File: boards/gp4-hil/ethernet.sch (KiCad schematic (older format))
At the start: 63 parts, among them J1 BEL_FUSE_0826-1G1T-23-F, J3 XILINX_JTAG_ICESIDE, J4 XILINX_JTAG_ICESIDE, U2 XC7A100T-1FTG256C, U29 TXB0104RUT, U30 TXB0104RUT, U33 125 MHz, U5 KSZ9031RN, U7 25 MHz

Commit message: Added pulldown on ETH_RESET_N to ensure PHY stays in reset until FPGA initializes
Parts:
- added R187: 10K, symbol R
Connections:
- net ETH_RESET_N: now also R187.2
- net GND: now also R187.1
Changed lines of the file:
@@
 	11700 8500 11900 8500
 Wire Wire Line
-	12100 8600 11200 8600
+	11200 8600 12800 8600
 Wire Wire Line
 	11200 8500 11400 8500
@@
 Connection ~ 6850 6150
 Connection ~ 7750 6150
+$Comp
+L R R187
+U 1 1 57747EB0
+P 12800 8750
+F 0 "R187" H 12650 8750 50  0000 C CNN
+F 1 "10K" V 12800 8750 50  0000 C CNN
+F 2 "" V 12730 8750 30  0000 C CNN
+F 3 "" H 12800 8750 30  0000 C CNN
+	1    12800 8750
+	-1   0    0    1
+$EndComp
+Text Label 12650 8900 2    60   ~ 0
+GND
+Wire Wire Line
+	12650 8900 12800 8900
 $EndSCHEMATC

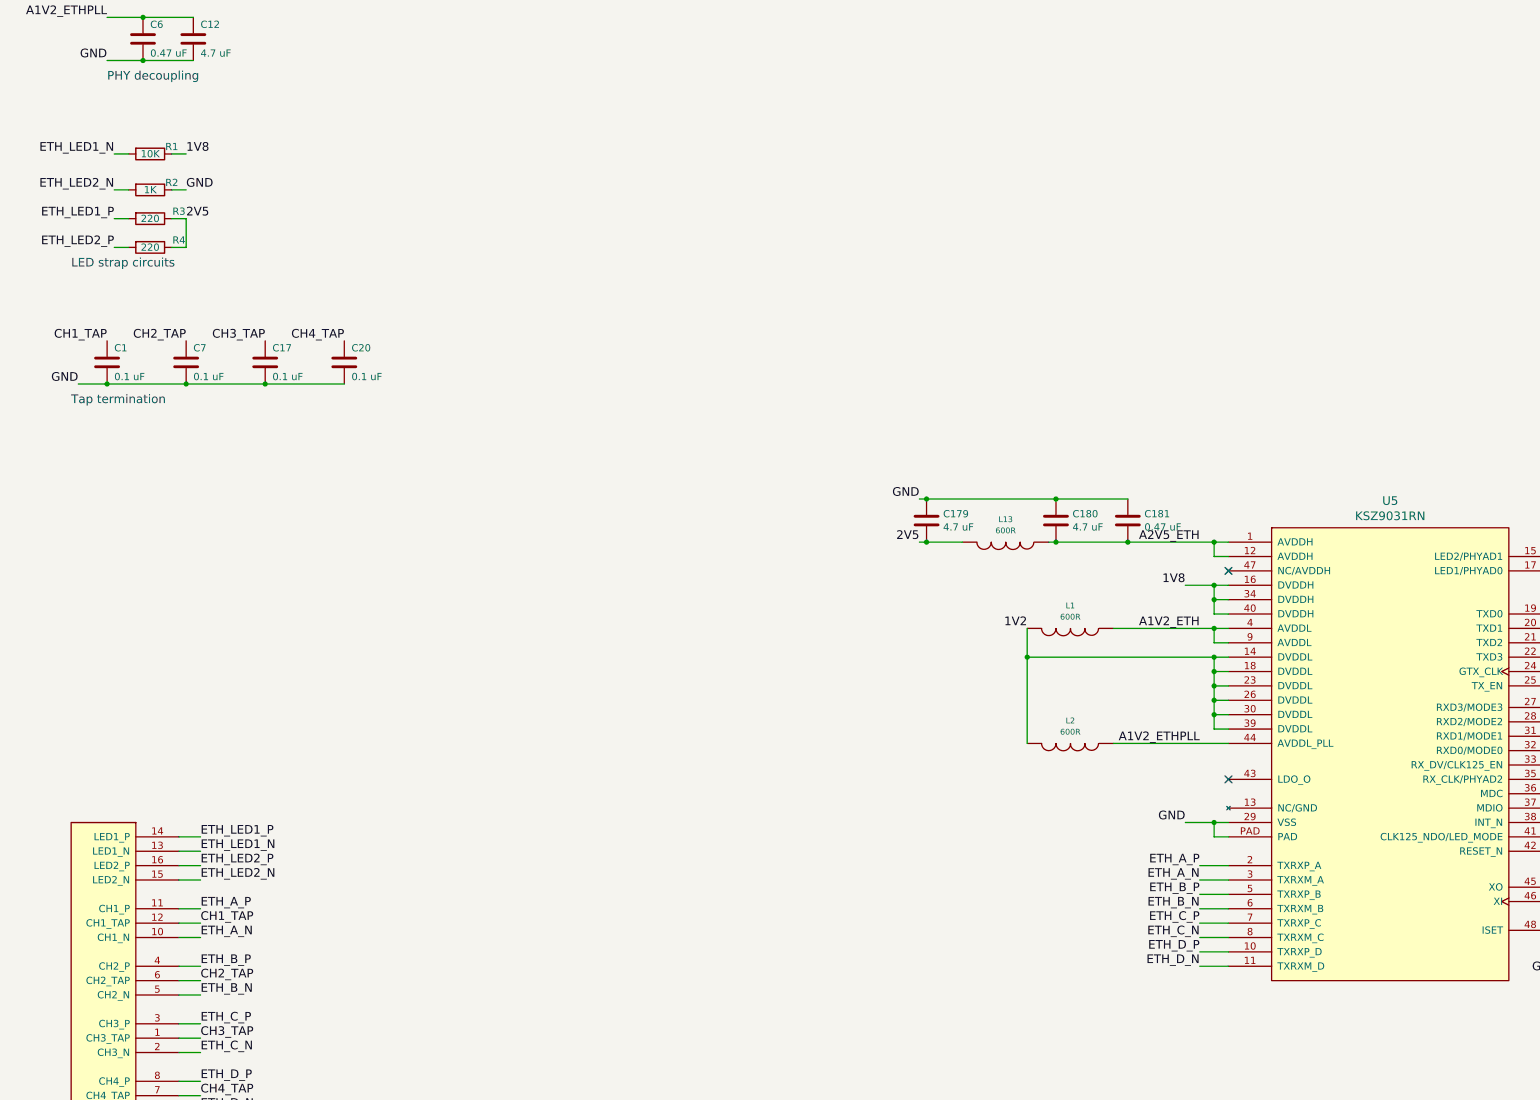
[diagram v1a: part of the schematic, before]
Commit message: Added PHY_MDC strap for PHY address configuration
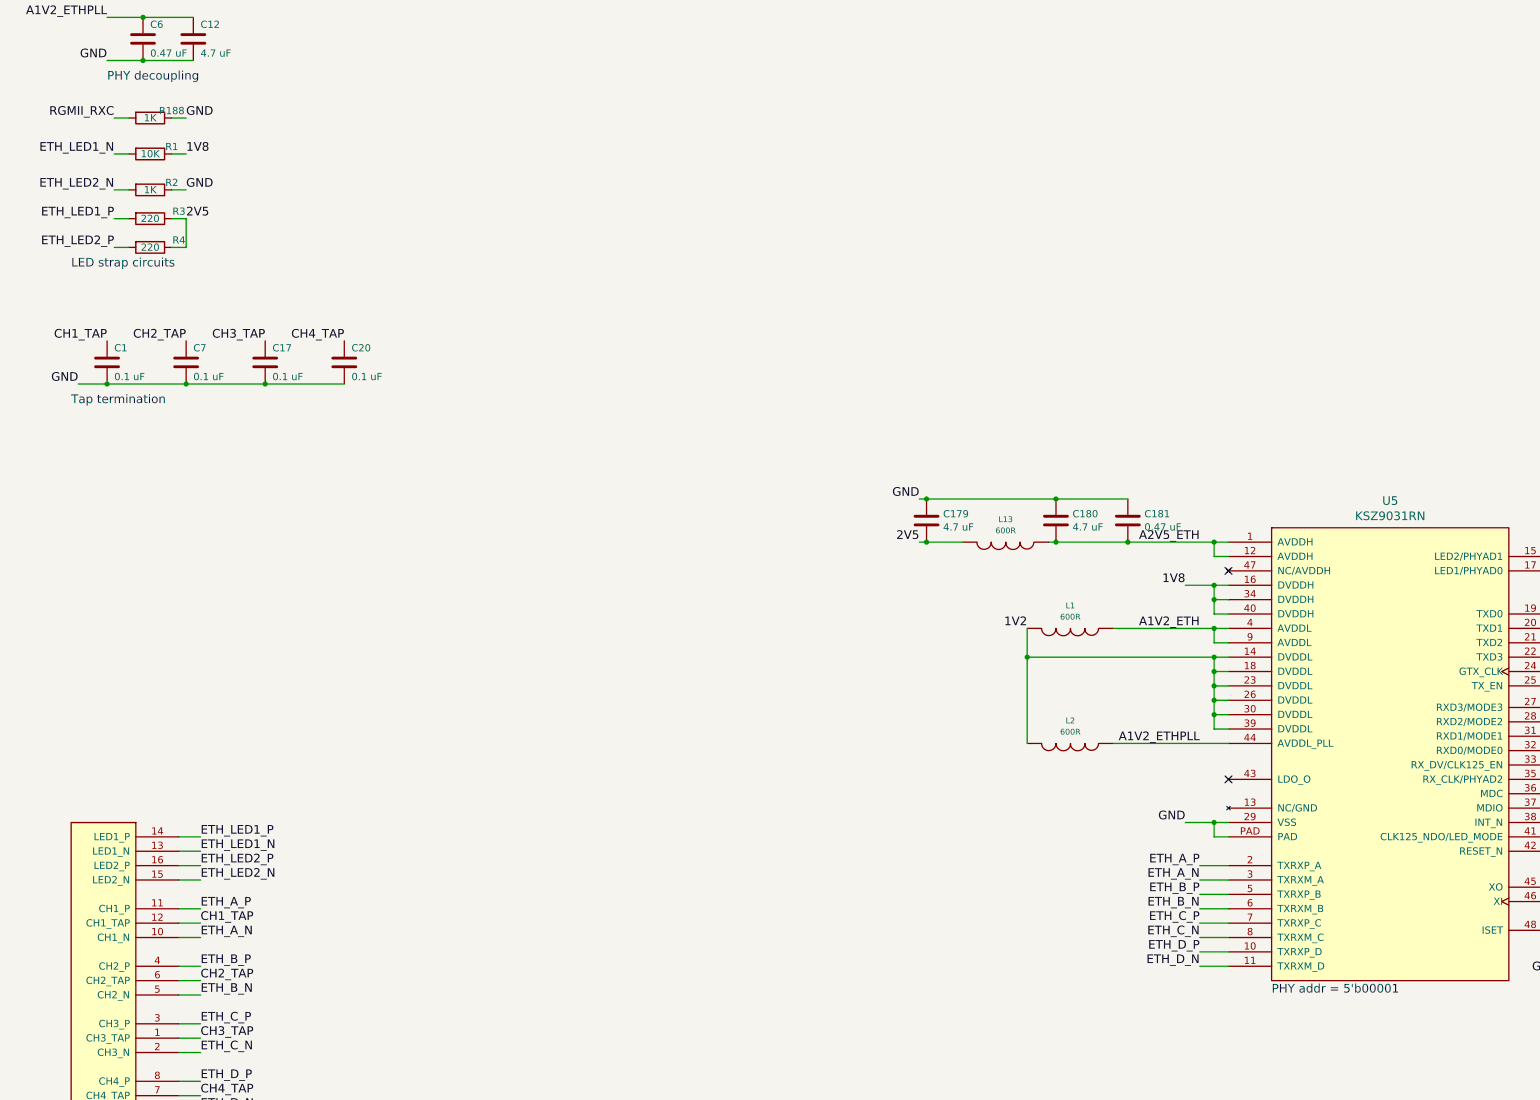
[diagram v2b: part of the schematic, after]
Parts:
- added R188: 1K, symbol R
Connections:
- net GND: now also R188.1
- net RGMII_RXC: now also R188.2
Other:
- note added: "PHY addr = 5'b00001"
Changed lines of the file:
@@
 Wire Wire Line
 	12650 8900 12800 8900
+Text Label 1200 3500 2    60   ~ 0
+RGMII_RXC
+$Comp
+L R R188
+U 1 1 57758CA7
+P 1450 3500
+F 0 "R188" V 1400 3650 50  0000 C CNN
+F 1 "1K" V 1450 3500 50  0000 C CNN
+F 2 "" V 1380 3500 30  0000 C CNN
+F 3 "" H 1450 3500 30  0000 C CNN
+	1    1450 3500
+	0    1    1    0
+$EndComp
+Wire Wire Line
+	1200 3500 1300 3500
+Text Label 1700 3500 0    60   ~ 0
+GND
+Wire Wire Line
+	1700 3500 1600 3500
+Text Notes 9250 9600 0    60   ~ 0
+PHY addr = 5'b00001
 $EndSCHEMATC

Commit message: Began work on footprint creation for layout.
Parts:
- C1, C10, C11, C14, C16, C163, C164, C165, C166, C17, C175, C181, C19, C2, C20, C21, C22, C24, C3, C4, C5, C6, C7, C8, C9: footprint (none) -> azonenberg_pcb:EIA_0402_CAP_NOSILK
- C12, C13, C15, C179, C18, C180, C23: footprint (none) -> azonenberg_pcb:EIA_0603_CAP_NOSILK
- J1: footprint (none) -> azonenberg_pcb:CONN_BELFUSE_0826_1G1T_23_F
- J3, J4: footprint (none) -> azonenberg_pcb:XILINX_JTAG_PTH_MOLEX_0878311420
- L1, L13, L2: footprint (none) -> azonenberg_pcb:EIA_0805_INDUCTOR_NOSILK
- TP22, TP23: footprint (none) -> azonenberg_pcb:TESTPOINT_SMT_KEYSTONE_5016
- U5: footprint (none) -> azonenberg_pcb:QFN_48_0.5MM_7x7MM

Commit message: Updated PCB with a lot more component footprints
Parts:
- L1, L13, L2: footprint azonenberg_pcb:EIA_0805_INDUCTOR_NOSILK -> azonenberg_pcb:EIA_0603_INDUCTOR_NOSILK
- R1, R10, R11, R12, R13, R14, R15, R150, R16, R187, R188, R2, R3, R4, R5, R6, R7, R8, R9: footprint (none) -> azonenberg_pcb:EIA_0402_RES_NOSILK
- U2: footprint (none) -> azonenberg_pcb:BGA_256_17x17_FULLARRAY_1MM
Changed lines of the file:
@@
 Sheet 3 7
 Title "GreenPak Hardware-In-Loop Test Platform"
-Date "2016-05-19"
+Date "2016-05-20"
 Rev "0.1"
 Comp "Andrew Zonenberg"
@@
 F 0 "R1" V 1400 3900 50  0000 C CNN
 F 1 "10K" V 1450 3750 50  0000 C CNN
-F 2 "" V 1380 3750 30  0001 C CNN
+F 2 "azonenberg_pcb:EIA_0402_RES_NOSILK" V 1380 3750 30  0001 C CNN
 F 3 "" H 1450 3750 30  0000 C CNN
 	1    1450 3750
@@
 F 0 "R2" V 1400 4150 50  0000 C CNN
 F 1 "1K" V 1450 4000 50  0000 C CNN
-F 2 "" V 1380 4000 30  0001 C CNN
+F 2 "azonenberg_pcb:EIA_0402_RES_NOSILK" V 1380 4000 30  0001 C CNN
 F 3 "" H 1450 4000 30  0000 C CNN
 	1    1450 4000
@@
 F 0 "R3" V 1400 4400 50  0000 C CNN
 F 1 "220" V 1450 4200 50  0000 C CNN
-F 2 "" V 1380 4200 30  0001 C CNN
+F 2 "azonenberg_pcb:EIA_0402_RES_NOSILK" V 1380 4200 30  0001 C CNN
 F 3 "" H 1450 4200 30  0000 C CNN
 	1    1450 4200
@@
 F 0 "R4" V 1400 4600 50  0000 C CNN
 F 1 "220" V 1450 4400 50  0000 C CNN
-F 2 "" V 1380 4400 30  0001 C CNN
+F 2 "azonenberg_pcb:EIA_0402_RES_NOSILK" V 1380 4400 30  0001 C CNN
 F 3 "" H 1450 4400 30  0000 C CNN
 	1    1450 4400
@@
 F 0 "L2" V 7692 7850 40  0000 C CNN
 F 1 "600R" V 7770 7850 40  0000 C CNN
-F 2 "azonenberg_pcb:EIA_0805_INDUCTOR_NOSILK" H 7850 7850 60  0001 C CNN
+F 2 "azonenberg_pcb:EIA_0603_INDUCTOR_NOSILK" H 7850 7850 60  0001 C CNN
 F 3 "" H 7850 7850 60  0000 C CNN
 	1    7850 7850
@@
 F 0 "L1" V 7692 7050 40  0000 C CNN
 F 1 "600R" V 7770 7050 40  0000 C CNN
-F 2 "azonenberg_pcb:EIA_0805_INDUCTOR_NOSILK" H 7850 7050 60  0001 C CNN
+F 2 "azonenberg_pcb:EIA_0603_INDUCTOR_NOSILK" H 7850 7050 60  0001 C CNN
 F 3 "" H 7850 7050 60  0000 C CNN
 	1    7850 7050
@@
 F 0 "R6" H 11470 9346 50  0000 L CNN
 F 1 "12.1k 1%" H 11470 9254 50  0000 L CNN
-F 2 "" V 11330 9300 30  0001 C CNN
+F 2 "azonenberg_pcb:EIA_0402_RES_NOSILK" V 11330 9300 30  0001 C CNN
 F 3 "" H 11400 9300 30  0000 C CNN
 	1    11400 9300
@@
 F 0 "R7" V 11500 7800 50  0000 C CNN
 F 1 "33" V 11550 7600 50  0000 C CNN
-F 2 "" V 11480 7600 30  0001 C CNN
+F 2 "azonenberg_pcb:EIA_0402_RES_NOSILK" V 11480 7600 30  0001 C CNN
 F 3 "" H 11550 7600 30  0000 C CNN
 	1    11550 7600
@@
 F 0 "R8" V 11500 7900 50  0000 C CNN
 F 1 "33" V 11550 7700 50  0000 C CNN
-F 2 "" V 11480 7700 30  0001 C CNN
+F 2 "azonenberg_pcb:EIA_0402_RES_NOSILK" V 11480 7700 30  0001 C CNN
 F 3 "" H 11550 7700 30  0000 C CNN
 	1    11550 7700
@@
 F 0 "R9" V 11500 8000 50  0000 C CNN
 F 1 "33" V 11550 7800 50  0000 C CNN
-F 2 "" V 11480 7800 30  0001 C CNN
+F 2 "azonenberg_pcb:EIA_0402_RES_NOSILK" V 11480 7800 30  0001 C CNN
 F 3 "" H 11550 7800 30  0000 C CNN
 	1    11550 7800
@@
 F 0 "R10" V 11500 8100 50  0000 C CNN
 F 1 "33" V 11550 7900 50  0000 C CNN
-F 2 "" V 11480 7900 30  0001 C CNN
+F 2 "azonenberg_pcb:EIA_0402_RES_NOSILK" V 11480 7900 30  0001 C CNN
 F 3 "" H 11550 7900 30  0000 C CNN
 	1    11550 7900
@@
 F 0 "R11" V 11500 8200 50  0000 C CNN
 F 1 "33" V 11550 8000 50  0000 C CNN
-F 2 "" V 11480 8000 30  0001 C CNN
+F 2 "azonenberg_pcb:EIA_0402_RES_NOSILK" V 11480 8000 30  0001 C CNN
 F 3 "" H 11550 8000 30  0000 C CNN
 	1    11550 8000
@@
 F 0 "R12" V 11500 8300 50  0000 C CNN
 F 1 "33" V 11550 8100 50  0000 C CNN
-F 2 "" V 11480 8100 30  0001 C CNN
+F 2 "azonenberg_pcb:EIA_0402_RES_NOSILK" V 11480 8100 30  0001 C CNN
 F 3 "" H 11550 8100 30  0000 C CNN
 	1    11550 8100
@@
 F 0 "R13" V 11500 8500 50  0000 C CNN
 F 1 "33" V 11550 8300 50  0000 C CNN
-F 2 "" V 11480 8300 30  0001 C CNN
+F 2 "azonenberg_pcb:EIA_0402_RES_NOSILK" V 11480 8300 30  0001 C CNN
 F 3 "" H 11550 8300 30  0000 C CNN
 	1    11550 8300
@@
 F 0 "R14" V 11500 8600 50  0000 C CNN
 F 1 "33" V 11550 8400 50  0000 C CNN
-F 2 "" V 11480 8400 30  0001 C CNN
+F 2 "azonenberg_pcb:EIA_0402_RES_NOSILK" V 11480 8400 30  0001 C CNN
 F 3 "" H 11550 8400 30  0000 C CNN
 	1    11550 8400
@@
 F 0 "R15" V 11500 8700 50  0000 C CNN
 F 1 "1K" V 11550 8500 50  0000 C CNN
-F 2 "" V 11480 8500 30  0001 C CNN
+F 2 "azonenberg_pcb:EIA_0402_RES_NOSILK" V 11480 8500 30  0001 C CNN
 F 3 "" H 11550 8500 30  0000 C CNN
 	1    11550 8500
@@
 F 0 "R5" V 10600 11350 50  0000 C CNN
 F 1 "33" V 10650 11150 50  0000 C CNN
-F 2 "" V 10580 11150 30  0001 C CNN
+F 2 "azonenberg_pcb:EIA_0402_RES_NOSILK" V 10580 11150 30  0001 C CNN
 F 3 "" H 10650 11150 30  0000 C CNN
 	1    10650 11150
@@
 F 0 "R16" V 15150 5500 50  0000 C CNN
 F 1 "1K" V 15250 5500 50  0000 C CNN
-F 2 "" V 15180 5500 30  0001 C CNN
+F 2 "azonenberg_pcb:EIA_0402_RES_NOSILK" V 15180 5500 30  0001 C CNN
 F 3 "" H 15250 5500 30  0000 C CNN
 	1    15250 5500
@@
 F 0 "U2" H 16400 9700 60  0000 L CNN
 F 1 "XC7A100T-1FTG256C" H 16400 9800 60  0000 L CNN
-F 2 "" H 16400 9900 60  0001 C CNN
+F 2 "azonenberg_pcb:BGA_256_17x17_FULLARRAY_1MM" H 16400 9900 60  0001 C CNN
 F 3 "" H 16400 9900 60  0000 C CNN
 	3    16400 9900
@@
 F 0 "R150" V 10600 12250 50  0000 C CNN
 F 1 "33" V 10650 12050 50  0000 C CNN
-F 2 "" V 10580 12050 30  0001 C CNN
+F 2 "azonenberg_pcb:EIA_0402_RES_NOSILK" V 10580 12050 30  0001 C CNN
 F 3 "" H 10650 12050 30  0000 C CNN
 	1    10650 12050
@@
 F 0 "L13" V 7242 6450 40  0000 C CNN
 F 1 "600R" V 7320 6450 40  0000 C CNN
-F 2 "azonenberg_pcb:EIA_0805_INDUCTOR_NOSILK" H 7400 6450 60  0001 C CNN
+F 2 "azonenberg_pcb:EIA_0603_INDUCTOR_NOSILK" H 7400 6450 60  0001 C CNN
 F 3 "" H 7400 6450 60  0000 C CNN
 	1    7400 6450
@@
 F 0 "R187" H 12650 8750 50  0000 C CNN
 F 1 "10K" V 12800 8750 50  0000 C CNN
-F 2 "" V 12730 8750 30  0001 C CNN
+F 2 "azonenberg_pcb:EIA_0402_RES_NOSILK" V 12730 8750 30  0001 C CNN
 F 3 "" H 12800 8750 30  0000 C CNN
 	1    12800 8750
@@
 F 0 "R188" V 1400 3650 50  0000 C CNN
 F 1 "1K" V 1450 3500 50  0000 C CNN
-F 2 "" V 1380 3500 30  0001 C CNN
+F 2 "azonenberg_pcb:EIA_0402_RES_NOSILK" V 1380 3500 30  0001 C CNN
 F 3 "" H 1450 3500 30  0000 C CNN
 	1    1450 3500

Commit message: Finished component footprints. Ready to begin layout.
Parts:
- U29, U30: footprint (none) -> azonenberg_pcb:QFN_12_0.4MM_2x2MM
- U33, U7: footprint (none) -> azonenberg_pcb:OSCILLATOR_2.0x1.6
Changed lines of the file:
@@
 Sheet 3 7
 Title "GreenPak Hardware-In-Loop Test Platform"
-Date "2016-05-20"
+Date "2016-05-22"
 Rev "0.1"
 Comp "Andrew Zonenberg"
@@
 F 0 "U7" H 9625 11437 60  0000 C CNN
 F 1 "25 MHz" H 9625 11331 60  0000 C CNN
-F 2 "" H 9650 11150 60  0001 C CNN
+F 2 "azonenberg_pcb:OSCILLATOR_2.0x1.6" H 9650 11150 60  0001 C CNN
 F 3 "" H 9650 11150 60  0000 C CNN
 	1    9650 11150
@@
 F 0 "U29" H 17425 13837 60  0000 C CNN
 F 1 "TXB0104RUT" H 17425 13731 60  0000 C CNN
-F 2 "" H 17400 12350 60  0001 C CNN
+F 2 "azonenberg_pcb:QFN_12_0.4MM_2x2MM" H 17400 12350 60  0001 C CNN
 F 3 "" H 17400 12350 60  0000 C CNN
 	1    17400 12350
@@
 F 0 "U30" H 17425 15887 60  0000 C CNN
 F 1 "TXB0104RUT" H 17425 15781 60  0000 C CNN
-F 2 "" H 17400 14400 60  0001 C CNN
+F 2 "azonenberg_pcb:QFN_12_0.4MM_2x2MM" H 17400 14400 60  0001 C CNN
 F 3 "" H 17400 14400 60  0000 C CNN
 	1    17400 14400
@@
 F 0 "U33" H 9625 12337 60  0000 C CNN
 F 1 "125 MHz" H 9625 12231 60  0000 C CNN
-F 2 "" H 9650 12050 60  0001 C CNN
+F 2 "azonenberg_pcb:OSCILLATOR_2.0x1.6" H 9650 12050 60  0001 C CNN
 F 3 "" H 9650 12050 60  0000 C CNN
 	1    9650 12050

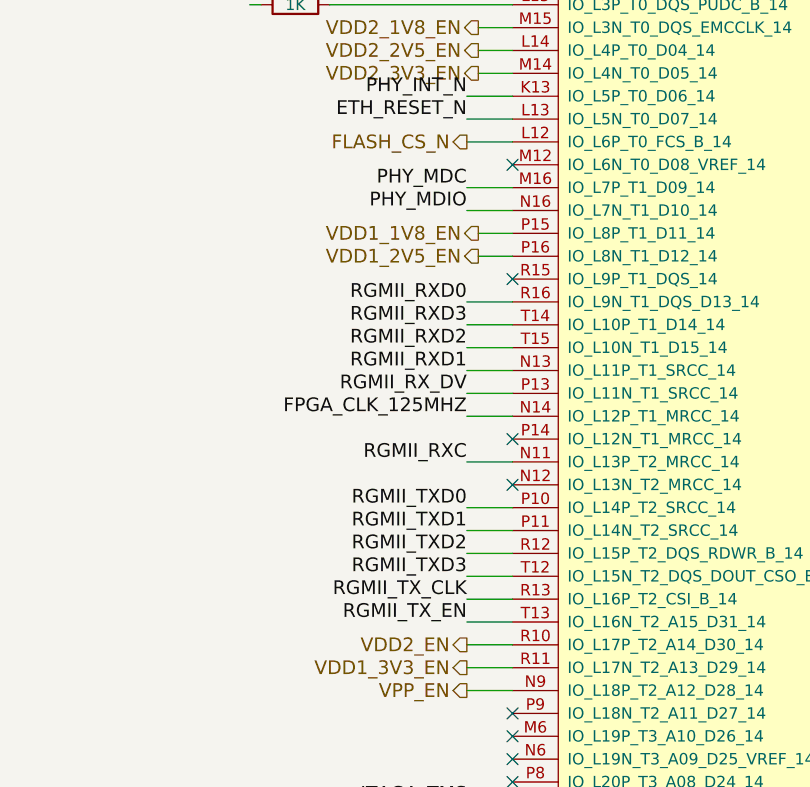
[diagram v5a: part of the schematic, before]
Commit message: Began routing RGMII bus
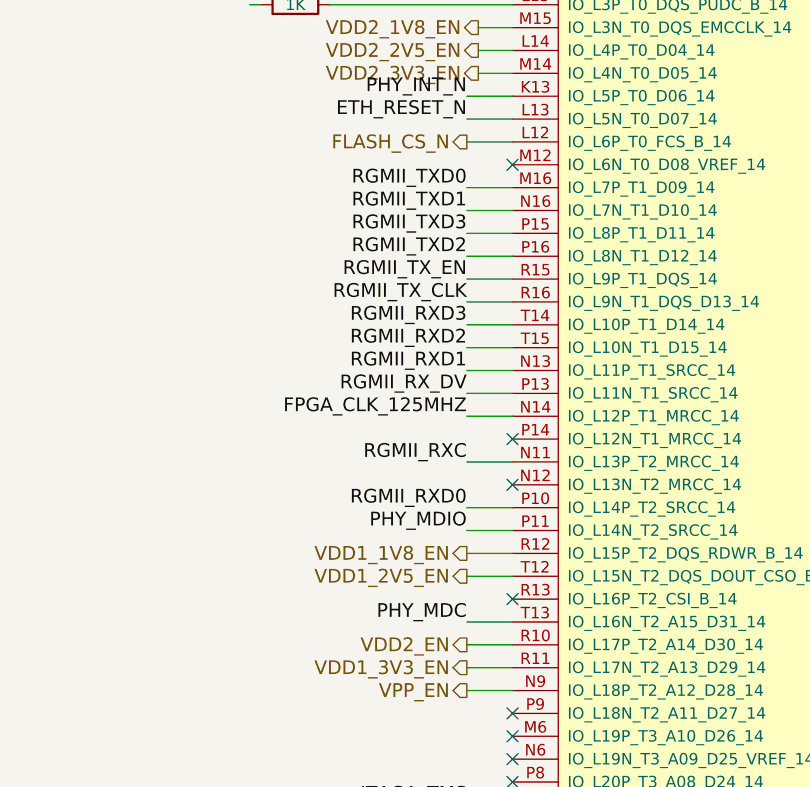
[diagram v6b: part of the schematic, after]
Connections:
- net PHY_MDC: now also U2.T13 (IO_L16N_T2_A15_D31_14); no longer U2.M16 (IO_L7P_T1_D09_14)
- net PHY_MDIO: now also U2.P11 (IO_L14N_T2_SRCC_14); no longer U2.N16 (IO_L7N_T1_D10_14)
- net RGMII_RXD0: now also U2.P10 (IO_L14P_T2_SRCC_14); no longer U2.R16 (IO_L9N_T1_DQS_D13_14)
- net RGMII_TXD0: now also U2.M16 (IO_L7P_T1_D09_14); no longer U2.P10 (IO_L14P_T2_SRCC_14)
- net RGMII_TXD1: now also U2.N16 (IO_L7N_T1_D10_14); no longer U2.P11 (IO_L14N_T2_SRCC_14)
- net RGMII_TXD2: now also U2.P16 (IO_L8N_T1_D12_14); no longer U2.R12 (IO_L15P_T2_DQS_RDWR_B_14)
- net RGMII_TXD3: now also U2.P15 (IO_L8P_T1_D11_14); no longer U2.T12 (IO_L15N_T2_DQS_DOUT_CSO_B_14)
- net RGMII_TX_CLK: now also U2.R16 (IO_L9N_T1_DQS_D13_14); no longer U2.R13 (IO_L16P_T2_CSI_B_14)
- net RGMII_TX_EN: now also U2.R15 (IO_L9P_T1_DQS_14); no longer U2.T13 (IO_L16N_T2_A15_D31_14)
- net VDD1_1V8_EN: now also U2.R12 (IO_L15P_T2_DQS_RDWR_B_14); no longer U2.P15 (IO_L8P_T1_D11_14)
- net VDD1_2V5_EN: now also U2.T12 (IO_L15N_T2_DQS_DOUT_CSO_B_14); no longer U2.P16 (IO_L8N_T1_D12_14)
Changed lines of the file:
@@
 Sheet 3 7
 Title "GreenPak Hardware-In-Loop Test Platform"
-Date "2016-05-22"
+Date "2016-05-23"
 Rev "0.1"
 Comp "Andrew Zonenberg"
@@
 Text Label 16000 7100 2    60   ~ 0
 RGMII_RXD1
-Text Label 16000 6800 2    60   ~ 0
+Text Label 16000 7700 2    60   ~ 0
 RGMII_RXD0
 Text Label 16000 7200 2    60   ~ 0
@@
 Text Label 16000 7500 2    60   ~ 0
 RGMII_RXC
-Text Label 16000 6300 2    60   ~ 0
+Text Label 16000 8200 2    60   ~ 0
 PHY_MDC
-Text Label 16000 6400 2    60   ~ 0
+Text Label 16000 7800 2    60   ~ 0
 PHY_MDIO
 Text Label 16000 5900 2    60   ~ 0
 PHY_INT_N
-Text Label 16000 7700 2    60   ~ 0
+Text Label 16000 6300 2    60   ~ 0
 RGMII_TXD0
-Text Label 16000 7800 2    60   ~ 0
+Text Label 16000 6400 2    60   ~ 0
 RGMII_TXD1
-Text Label 16000 7900 2    60   ~ 0
+Text Label 16000 6600 2    60   ~ 0
 RGMII_TXD2
-Text Label 16000 8000 2    60   ~ 0
+Text Label 16000 6500 2    60   ~ 0
 RGMII_TXD3
-Text Label 16000 8100 2    60   ~ 0
+Text Label 16000 6800 2    60   ~ 0
 RGMII_TX_CLK
-Text Label 16000 8200 2    60   ~ 0
+Text Label 16000 6700 2    60   ~ 0
 RGMII_TX_EN
 Text Label 16000 6000 2    60   ~ 0
@@
 Text HLabel 16000 8400 0    60   Output ~ 0
 VDD1_3V3_EN
-Text HLabel 16050 6600 0    60   Output ~ 0
+Text HLabel 16000 8000 0    60   Output ~ 0
 VDD1_2V5_EN
-Text HLabel 16050 6500 0    60   Output ~ 0
+Text HLabel 16000 7900 0    60   Output ~ 0
 VDD1_1V8_EN
 Text HLabel 16050 5800 0    60   Output ~ 0
@@
 	16000 8200 16200 8200
 Wire Wire Line
-	16200 8100 16000 8100
-Wire Wire Line
 	16000 8000 16200 8000
 Wire Wire Line
@@
 	16200 5800 16050 5800
 Wire Wire Line
-	16050 6500 16200 6500
-Wire Wire Line
-	16200 6600 16050 6600
+	16000 6500 16200 6500
+Wire Wire Line
+	16000 6600 16200 6600
 Wire Wire Line
 	16000 6800 16200 6800
@@
 Wire Wire Line
 	16200 6900 16000 6900
-NoConn ~ 16200 6700
 Wire Wire Line
 	16200 8400 16000 8400
@@
 Text Notes 9250 9600 0    60   ~ 0
 PHY addr = 5'b00001
+Wire Wire Line
+	16200 6700 16000 6700
+NoConn ~ 16200 8100
 $EndSCHEMATC
